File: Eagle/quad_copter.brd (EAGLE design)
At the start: 100 x 80 mm, 12 parts, among them X1 STM32F4_DISC

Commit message: first brd commit
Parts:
- moved USART1 164.0 mm to (69.8, 10.2), turned to 270 degrees
- moved X1 147.6 mm to (95.2, 54.6), turned to 270 degrees
- moved JUM1 137.3 mm to (6.35, 16.5), turned to 90 degrees
- moved USART2 129.6 mm to (108.0, 99.1)
- moved JUM4 123.4 mm to (33.0, 16.5), turned to 90 degrees
- moved JUM3 110.7 mm to (24.1, 16.5), turned to 90 degrees
- moved USART3 106.7 mm to (71.1, 99.1)
- moved JUM2 100.9 mm to (15.2, 16.5), turned to 90 degrees
- moved BEC1 39.5 mm to (6.35, 6.35), turned to 180 degrees
- moved BEC4 25.0 mm to (33.0, 6.35), turned to 180 degrees
- moved BEC3 15.9 mm to (24.1, 6.35), turned to 180 degrees
- moved BEC2 9.25 mm to (15.2, 6.35), turned to 180 degrees
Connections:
- net N$10: now also JUM3.1; no longer JUM2.1
- net N$11: now also JUM2.1; no longer JUM4.1
- net N$9: now also JUM4.1; no longer JUM3.1
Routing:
- net +5V: track 0.00 -> 318.8 mm, vias 0 -> 6
- net 0V: track 0.00 -> 166.4 mm, vias 0 -> 2
- net N$17: track 0.00 -> 139.7 mm
- net N$16: track 0.00 -> 123.2 mm
- net N$5: track 0.00 -> 82.5 mm, vias 0 -> 2
- net N$4: track 0.00 -> 81.3 mm, vias 0 -> 2
- net N$15: track 0.00 -> 73.7 mm
- net N$1: track 0.00 -> 71.1 mm, vias 0 -> 2
- net N$14: track 0.00 -> 57.1 mm
- net N$6: track 0.00 -> 29.2 mm
- net N$3: track 0.00 -> 25.4 mm, vias 0 -> 2
- net N$2: track 0.00 -> 20.3 mm
- net N$9: track 0.00 -> 8.89 mm
- net N$12: track 0.00 -> 8.89 mm
- net N$11: track 0.00 -> 8.89 mm
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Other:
- board size 100 x 80 mm -> 173.7 x 139.7 mm

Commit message: new scheme and board
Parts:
- moved USART3 99.2 mm to (48.3, 2.54), turned to 180 degrees
- moved USART2 63.5 mm to (86.4, 39.4), turned to 270 degrees
- moved BEC4 49.3 mm to (5.08, 47.0), turned to 90 degrees
- moved X1 46.6 mm to (50.8, 40.6), turned to 0 degrees
- moved BEC3 35.9 mm to (5.08, 36.8), turned to 90 degrees
- moved JUM4 34.5 mm to (12.7, 44.5), turned to 0 degrees
- moved JUM3 23.3 mm to (12.7, 36.8), turned to 0 degrees
- moved BEC2 22.7 mm to (5.08, 26.7), turned to 90 degrees
- moved USART1 18.9 mm to (87.6, 16.5)
- moved JUM2 10.5 mm to (12.7, 26.7), turned to 0 degrees
- moved BEC1 10.2 mm to (5.08, 16.5), turned to 90 degrees
- moved JUM1 6.35 mm to (12.7, 16.5), turned to 0 degrees
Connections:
- removed net N$6: USART3.3, X1.L33
- new net N$13: USART2.3, X1.R28
- net 0V: now also X1.L49, X1.L50, X1.R49, X1.R50; no longer X1.T4
- net GND: now also X1.T4; no longer X1.L49, X1.L50, X1.R49, X1.R50
- net N$1: now also USART3.3, X1.L39; no longer USART2.2, X1.L14
- net N$14: now also X1.L21; no longer X1.R46
- net N$15: now also X1.L22; no longer X1.R47
- net N$2: now also USART3.2, X1.L40; no longer USART2.3, X1.L11
- net N$5: now also USART2.2, X1.R37; no longer USART3.2, X1.L34
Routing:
- net N$17: track 139.7 -> 19.1 mm
- net N$16: track 123.2 -> 54.6 mm, vias 0 -> 2
- net GND: track 5.08 -> 58.4 mm
- net N$4: track 81.3 -> 39.4 mm, vias 2 -> 0
- net N$14: track 57.1 -> 22.2 mm, vias 0 -> 2
- net N$15: track 73.7 -> 107.9 mm, vias 0 -> 2
- net N$6: track 29.2 -> 0.00 mm
- net N$2: track 20.3 -> 41.5 mm, vias 0 -> 2
- net 0V: track 166.4 -> 151.1 mm, vias 2 -> 4
- net N$3: track 25.4 -> 11.4 mm, vias 2 -> 0
- net N$5: track 82.5 -> 94.0 mm, vias 2 -> 0
- net N$13: track 0.00 -> 10.2 mm
- net N$1: track 71.1 -> 67.6 mm
- net +5V: track 318.8 -> 321.6 mm, vias 6 -> 2
- net N$12: track 8.89 -> 6.35 mm
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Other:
- board size 173.7 x 139.7 mm -> 97.8 x 111.4 mm

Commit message: 2nd version of board
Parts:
- moved BEC2 1.27 mm to (5.08, 25.4)
- moved BEC4 1.27 mm to (5.08, 45.7)
- moved JUM2 1.27 mm to (12.7, 25.4)
- moved BEC1 1.27 mm to (5.08, 15.2)
- moved JUM1 1.27 mm to (12.7, 15.2)
- moved BEC3 1.27 mm to (5.08, 35.6)
- moved JUM3 1.27 mm to (12.7, 35.6)
- moved JUM4 1.27 mm to (12.7, 45.7)
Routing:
- net +5V: track 321.6 -> 309.9 mm
- net N$19: track 0.00 -> 11.4 mm
- net N$6: track 0.00 -> 10.2 mm
- net N$8: track 0.00 -> 10.0 mm
- net N$18: track 0.00 -> 7.46 mm
- net N$1: track 67.6 -> 63.7 mm
- net N$17: track 19.1 -> 17.8 mm
- net N$16: track 54.6 -> 53.3 mm
- net N$15: track 107.9 -> 106.7 mm
- net 0V: track 151.1 -> 149.9 mm
- net N$2: track 41.5 -> 42.4 mm
- net N$14: track 22.2 -> 22.9 mm

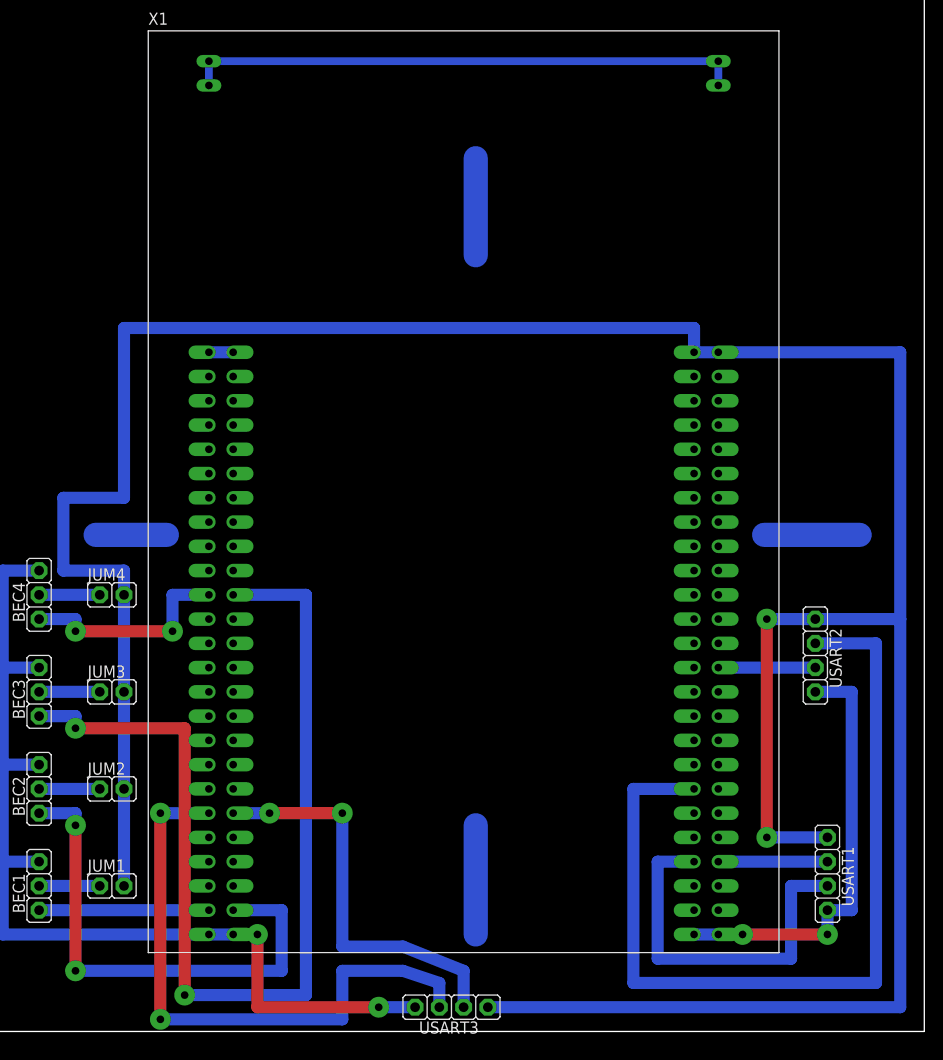
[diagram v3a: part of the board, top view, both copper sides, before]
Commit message: Improved board layout
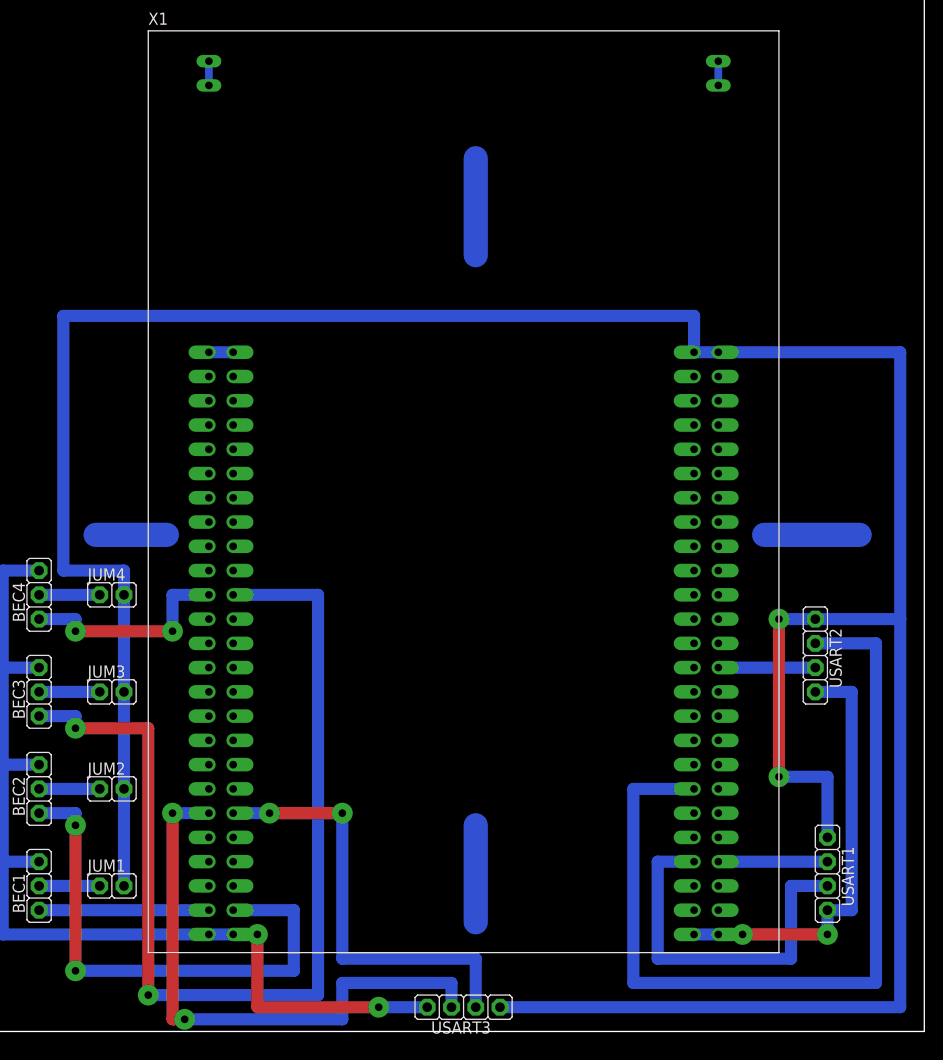
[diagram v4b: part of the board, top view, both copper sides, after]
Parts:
- moved USART3 1.27 mm to (49.5, 2.54)
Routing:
- net GND: track 58.4 -> 5.08 mm
- net N$2: track 42.4 -> 45.7 mm
- net N$1: track 63.7 -> 61.0 mm
- net N$16: track 53.3 -> 55.9 mm
- net N$15: track 106.7 -> 109.2 mm
- net N$19: track 11.4 -> 10.2 mm
- net 0V: track 149.9 -> 151.1 mm
- net +5V: track 309.9 -> 308.6 mm
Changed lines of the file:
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@@
 <element name="JUM4" library="#PaJa_konektory" package="S1G2_JUM" value="S1G2_JUMP" x="12.7" y="45.72"/>
 <element name="JUM2" library="#PaJa_konektory" package="S1G2_JUM" value="S1G2_JUMP" x="12.7" y="25.4"/>
-<element name="USART3" library="#PaJa_konektory" package="S1G4_JUM" value="S1G4_JUMP" x="48.26" y="2.54" rot="R180"/>
+<element name="USART3" library="#PaJa_konektory" package="S1G4_JUM" value="S1G4_JUMP" x="49.53" y="2.54" rot="R180"/>
 </elements>
 <signals>
@@
 <wire x1="22.86" y1="99.06" x2="22.86" y2="101.6" width="0.8128" layer="16"/>
 <wire x1="76.2" y1="99.06" x2="76.2" y2="101.6" width="0.8128" layer="16"/>
-<wire x1="22.86" y1="101.6" x2="76.2" y2="101.6" width="0.8128" layer="16"/>
+<wire x1="22.86" y1="101.6" x2="76.2" y2="101.6" width="0" layer="19" extent="1-16"/>
 <contactref element="X1" pad="T1"/>
 <contactref element="X1" pad="T2"/>
@@
 <wire x1="13.97" y1="25.4" x2="13.97" y2="35.56" width="1.27" layer="16"/>
 <wire x1="13.97" y1="35.56" x2="13.97" y2="45.72" width="1.27" layer="16"/>
-<wire x1="13.97" y1="73.66" x2="73.66" y2="73.66" width="1.27" layer="16"/>
-<wire x1="73.66" y1="73.66" x2="73.66" y2="71.12" width="1.27" layer="16"/>
+<wire x1="7.62" y1="74.93" x2="73.66" y2="74.93" width="1.27" layer="16"/>
+<wire x1="73.66" y1="74.93" x2="73.66" y2="71.12" width="1.27" layer="16"/>
 <wire x1="73.66" y1="71.12" x2="76.2" y2="71.12" width="1.27" layer="16"/>
-<wire x1="87.63" y1="20.32" x2="81.28" y2="20.32" width="1.27" layer="16"/>
-<via x="81.28" y="20.32" extent="1-16" drill="0.8" diameter="2.1844" shape="square"/>
-<wire x1="81.28" y1="20.32" x2="81.28" y2="43.18" width="1.27" layer="1"/>
-<via x="81.28" y="43.18" extent="1-16" drill="0.8" diameter="2.1844" shape="square"/>
-<wire x1="86.36" y1="43.18" x2="81.28" y2="43.18" width="1.27" layer="16"/>
+<wire x1="87.63" y1="20.32" x2="87.63" y2="26.67" width="1.27" layer="16"/>
+<wire x1="87.63" y1="26.67" x2="82.55" y2="26.67" width="1.27" layer="16"/>
+<via x="82.55" y="26.67" extent="1-16" drill="0.8" diameter="2.1844" shape="square"/>
+<wire x1="82.55" y1="26.67" x2="82.55" y2="43.18" width="1.27" layer="1"/>
+<via x="82.55" y="43.18" extent="1-16" drill="0.8" diameter="2.1844" shape="square"/>
+<wire x1="86.36" y1="43.18" x2="82.55" y2="43.18" width="1.27" layer="16"/>
 <contactref element="USART3" pad="1"/>
-<wire x1="52.07" y1="2.54" x2="95.25" y2="2.54" width="1.27" layer="16"/>
+<wire x1="53.34" y1="2.54" x2="95.25" y2="2.54" width="1.27" layer="16"/>
 <wire x1="95.25" y1="2.54" x2="95.25" y2="43.18" width="1.27" layer="16"/>
 <wire x1="95.25" y1="43.18" x2="86.36" y2="43.18" width="1.27" layer="16"/>
 <wire x1="13.97" y1="45.72" x2="13.97" y2="48.26" width="1.27" layer="16"/>
-<wire x1="13.97" y1="55.88" x2="13.97" y2="73.66" width="1.27" layer="16"/>
 <wire x1="13.97" y1="48.26" x2="7.62" y2="48.26" width="1.27" layer="16"/>
-<wire x1="7.62" y1="48.26" x2="7.62" y2="55.88" width="1.27" layer="16"/>
-<wire x1="7.62" y1="55.88" x2="13.97" y2="55.88" width="1.27" layer="16"/>
+<wire x1="7.62" y1="48.26" x2="7.62" y2="74.93" width="1.27" layer="16"/>
 <wire x1="76.2" y1="71.12" x2="95.25" y2="71.12" width="1.27" layer="16"/>
 <wire x1="95.25" y1="71.12" x2="95.25" y2="43.18" width="1.27" layer="16"/>
@@
 <wire x1="87.63" y1="10.16" x2="87.63" y2="12.7" width="1.27" layer="16"/>
 <contactref element="USART3" pad="4"/>
-<wire x1="44.45" y1="2.54" x2="40.64" y2="2.54" width="1.27" layer="16"/>
+<wire x1="45.72" y1="2.54" x2="40.64" y2="2.54" width="1.27" layer="16"/>
 <via x="40.64" y="2.54" extent="1-16" drill="0.8" diameter="2.1844" shape="square"/>
 <wire x1="40.64" y1="2.54" x2="27.94" y2="2.54" width="1.27" layer="1"/>
@@
 <wire x1="1.27" y1="10.16" x2="1.27" y2="17.78" width="1.27" layer="16"/>
 <wire x1="5.08" y1="48.26" x2="22.86" y2="68.58" width="0" layer="19" extent="1-1"/>
-<wire x1="73.66" y1="10.16" x2="44.45" y2="2.54" width="0" layer="19" extent="1-1"/>
+<wire x1="73.66" y1="10.16" x2="45.72" y2="2.54" width="0" layer="19" extent="1-1"/>
 </signal>
 <signal name="N$3">
@@
 <contactref element="BEC3" pad="1"/>
 <contactref element="X1" pad="L22"/>
-<via x="20.32" y="3.81" extent="1-16" drill="0.8" diameter="2.1844" shape="square"/>
-<wire x1="20.32" y1="3.81" x2="33.02" y2="3.81" width="1.27" layer="16"/>
-<wire x1="33.02" y1="3.81" x2="33.02" y2="45.72" width="1.27" layer="16"/>
-<wire x1="33.02" y1="45.72" x2="25.4" y2="45.72" width="1.27" layer="16"/>
-<wire x1="20.32" y1="3.81" x2="20.32" y2="31.75" width="1.27" layer="1"/>
-<wire x1="20.32" y1="31.75" x2="8.89" y2="31.75" width="1.27" layer="1"/>
+<via x="16.51" y="3.81" extent="1-16" drill="0.8" diameter="2.1844" shape="square"/>
+<wire x1="16.51" y1="3.81" x2="34.29" y2="3.81" width="1.27" layer="16"/>
+<wire x1="34.29" y1="3.81" x2="34.29" y2="45.72" width="1.27" layer="16"/>
+<wire x1="34.29" y1="45.72" x2="25.4" y2="45.72" width="1.27" layer="16"/>
+<wire x1="16.51" y1="3.81" x2="16.51" y2="31.75" width="1.27" layer="1"/>
+<wire x1="16.51" y1="31.75" x2="8.89" y2="31.75" width="1.27" layer="1"/>
 <via x="8.89" y="31.75" extent="1-16" drill="0.8" diameter="2.1844" shape="square"/>
 <wire x1="8.89" y1="31.75" x2="8.89" y2="33.02" width="1.27" layer="16"/>
@@
 <contactref element="BEC2" pad="1"/>
 <contactref element="X1" pad="L48"/>
-<wire x1="25.4" y1="12.7" x2="30.48" y2="12.7" width="1.27" layer="16"/>
-<wire x1="30.48" y1="12.7" x2="30.48" y2="6.35" width="1.27" layer="16"/>
-<wire x1="30.48" y1="6.35" x2="8.89" y2="6.35" width="1.27" layer="16"/>
+<wire x1="25.4" y1="12.7" x2="31.75" y2="12.7" width="1.27" layer="16"/>
+<wire x1="31.75" y1="12.7" x2="31.75" y2="6.35" width="1.27" layer="16"/>
+<wire x1="31.75" y1="6.35" x2="8.89" y2="6.35" width="1.27" layer="16"/>
 <via x="8.89" y="6.35" extent="1-16" drill="0.8" diameter="2.1844" shape="square"/>
 <wire x1="8.89" y1="6.35" x2="8.89" y2="21.59" width="1.27" layer="1"/>
@@
 <contactref element="X1" pad="L39"/>
 <contactref element="USART3" pad="3"/>
-<wire x1="22.86" y1="22.86" x2="17.78" y2="22.86" width="1.27" layer="16"/>
-<via x="17.78" y="22.86" extent="1-16" drill="0.8" diameter="2.1844" shape="square"/>
-<wire x1="17.78" y1="22.86" x2="17.78" y2="1.27" width="1.27" layer="1"/>
-<via x="17.78" y="1.27" extent="1-16" drill="0.8" diameter="2.1844" shape="square"/>
-<wire x1="17.78" y1="1.27" x2="36.83" y2="1.27" width="1.27" layer="16"/>
-<wire x1="36.83" y1="1.27" x2="36.83" y2="6.35" width="1.27" layer="16"/>
-<wire x1="36.83" y1="6.35" x2="43.18" y2="6.35" width="1.27" layer="16"/>
-<wire x1="43.18" y1="6.35" x2="46.99" y2="5.08" width="1.27" layer="16"/>
-<wire x1="46.99" y1="5.08" x2="46.99" y2="2.54" width="1.27" layer="16"/>
+<wire x1="22.86" y1="22.86" x2="19.05" y2="22.86" width="1.27" layer="16"/>
+<via x="19.05" y="22.86" extent="1-16" drill="0.8" diameter="2.1844" shape="square"/>
+<wire x1="19.05" y1="22.86" x2="19.05" y2="1.27" width="1.27" layer="1"/>
+<wire x1="19.05" y1="1.27" x2="20.32" y2="1.27" width="1.27" layer="1"/>
+<via x="20.32" y="1.27" extent="1-16" drill="0.8" diameter="2.1844" shape="square"/>
+<wire x1="20.32" y1="1.27" x2="36.83" y2="1.27" width="1.27" layer="16"/>
+<wire x1="36.83" y1="1.27" x2="36.83" y2="5.08" width="1.27" layer="16"/>
+<wire x1="36.83" y1="5.08" x2="48.26" y2="5.08" width="1.27" layer="16"/>
+<wire x1="48.26" y1="5.08" x2="48.26" y2="2.54" width="1.27" layer="16"/>
 </signal>
 <signal name="N$2">
 <contactref element="USART3" pad="2"/>
 <contactref element="X1" pad="L40"/>
-<wire x1="49.53" y1="2.54" x2="49.53" y2="6.35" width="1.27" layer="16"/>
-<wire x1="49.53" y1="6.35" x2="43.18" y2="8.89" width="1.27" layer="16"/>
-<wire x1="43.18" y1="8.89" x2="36.83" y2="8.89" width="1.27" layer="16"/>
-<wire x1="36.83" y1="8.89" x2="36.83" y2="22.86" width="1.27" layer="16"/>
+<wire x1="50.8" y1="2.54" x2="50.8" y2="7.62" width="1.27" layer="16"/>
+<wire x1="50.8" y1="7.62" x2="36.83" y2="7.62" width="1.27" layer="16"/>
+<wire x1="36.83" y1="7.62" x2="36.83" y2="22.86" width="1.27" layer="16"/>
 <via x="36.83" y="22.86" extent="1-16" drill="0.8" diameter="2.1844" shape="square"/>
 <wire x1="36.83" y1="22.86" x2="29.21" y2="22.86" width="1.27" layer="1"/>
@@
 </signal>
 <signal name="N$19">
-<wire x1="50.8" y1="10.16" x2="50.8" y2="21.59" width="2.54" layer="16"/>
+<wire x1="50.8" y1="11.43" x2="50.8" y2="21.59" width="2.54" layer="16"/>
 </signal>
 </signals>

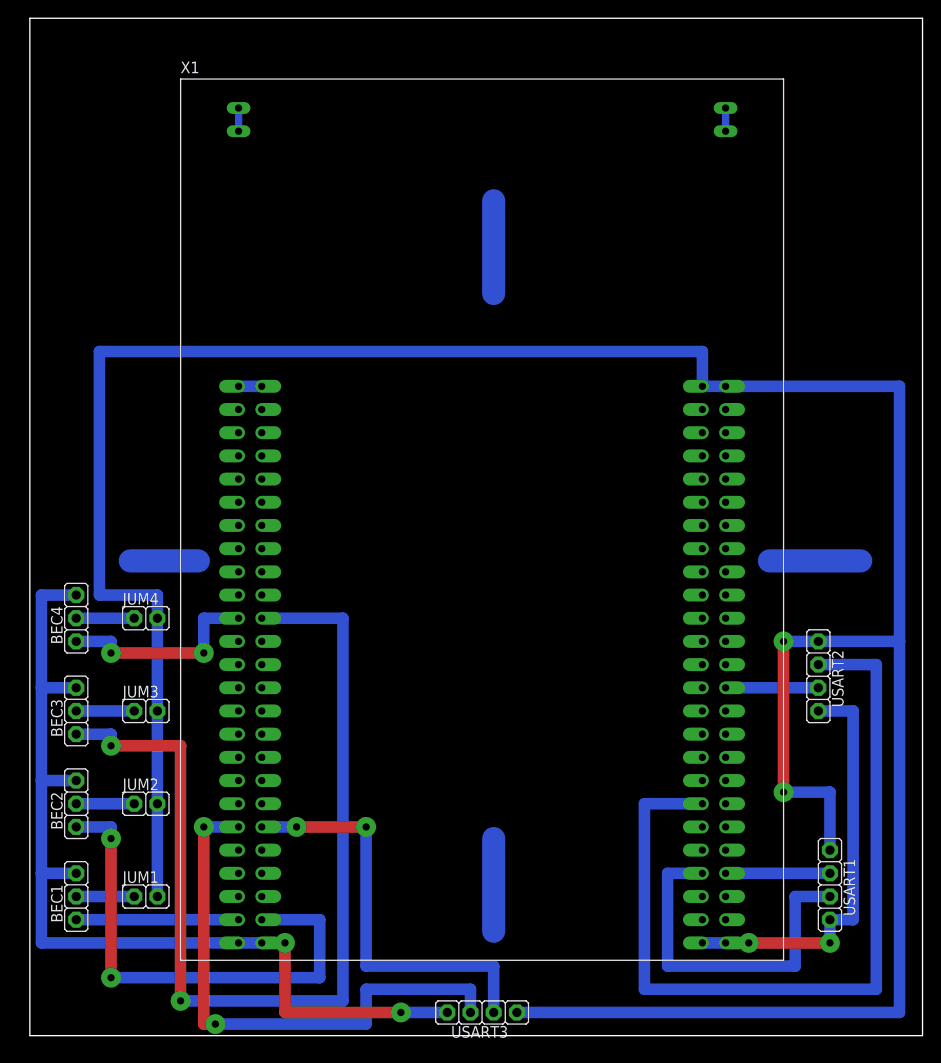
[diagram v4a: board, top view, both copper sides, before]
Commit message: Added connector to board
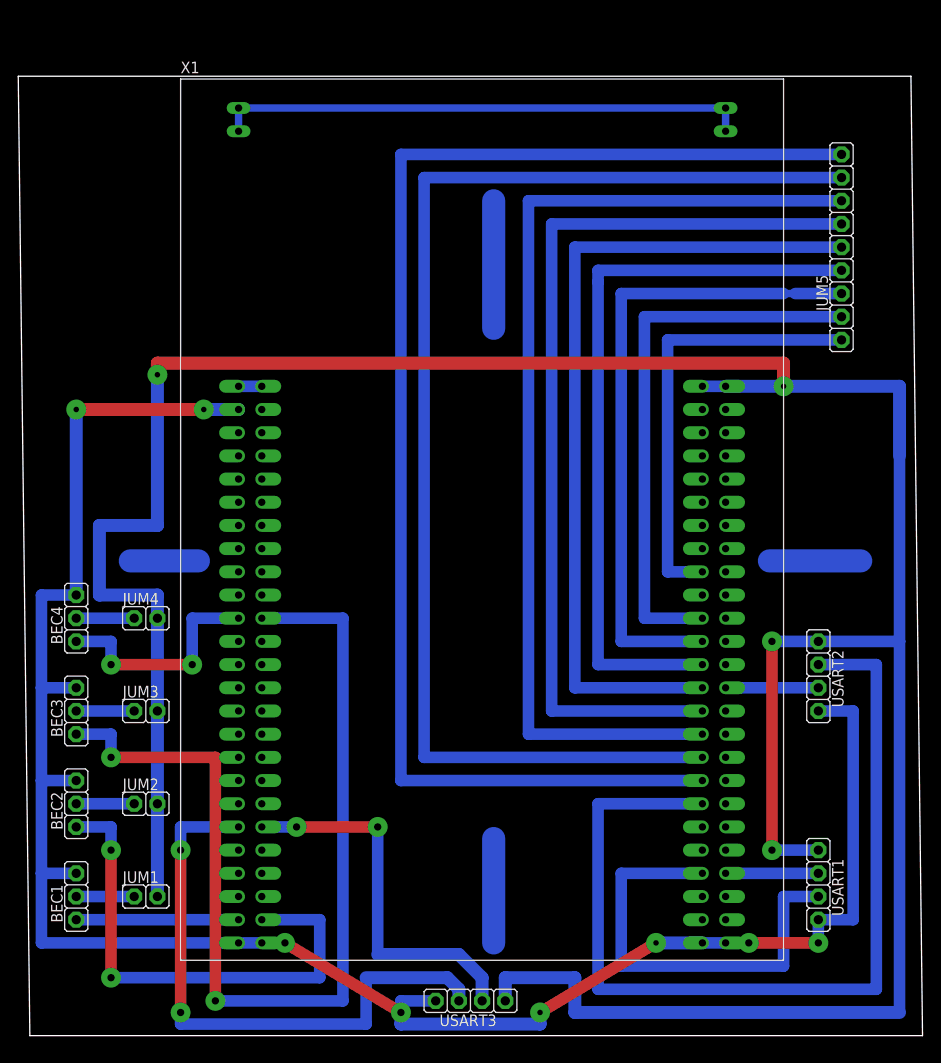
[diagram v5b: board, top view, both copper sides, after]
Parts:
- added JUM5: S1G9_JUMP, #PaJa_konektory:S1G9_JUM
- moved USART3 1.80 mm to (48.3, 3.81)
- moved USART1 1.27 mm to (86.4, 16.5)
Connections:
- new net N$20: JUM5.9, X1.R35
- new net N$21: JUM5.8, X1.R33
- new net N$22: JUM5.6, X1.R29
- new net N$23: JUM5.5, X1.R27
- new net N$24: JUM5.4, X1.R25
- new net N$25: JUM5.7, X1.R31
- new net N$27: JUM5.3, X1.R23
- new net N$28: JUM5.1, X1.R17
- new net N$29: JUM5.2, X1.R21
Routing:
- net N$20: track 0.00 -> 149.9 mm
- net N$21: track 0.00 -> 139.7 mm
- net N$25: track 0.00 -> 111.8 mm
- net N$22: track 0.00 -> 101.6 mm
- net N$23: track 0.00 -> 91.4 mm
- net N$24: track 0.00 -> 81.3 mm
- net N$27: track 0.00 -> 71.1 mm
- net 0V: track 151.1 -> 221.4 mm, vias 4 -> 8
- net N$29: track 0.00 -> 61.0 mm
- net GND: track 5.08 -> 58.4 mm
- net N$28: track 0.00 -> 48.3 mm
- net +5V: track 308.6 -> 356.9 mm, vias 2 -> 4
- net N$5: track 94.0 -> 104.1 mm
- net N$4: track 39.4 -> 48.3 mm
- net N$1: track 61.0 -> 65.3 mm
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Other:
- board size 97.8 x 111.4 mm -> 99 x 105.1 mm
